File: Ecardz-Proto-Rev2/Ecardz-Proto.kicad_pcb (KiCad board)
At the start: 4 copper layers, 110 x 90 mm, 63 parts, among them IC1 M24LR04E-RMN6T/2, J1 Conn_02x06_Odd_Even, J2 Conn_01x24, J3 Conn_01x06, Q1 NMOS, U1 STM32L071K8Ux

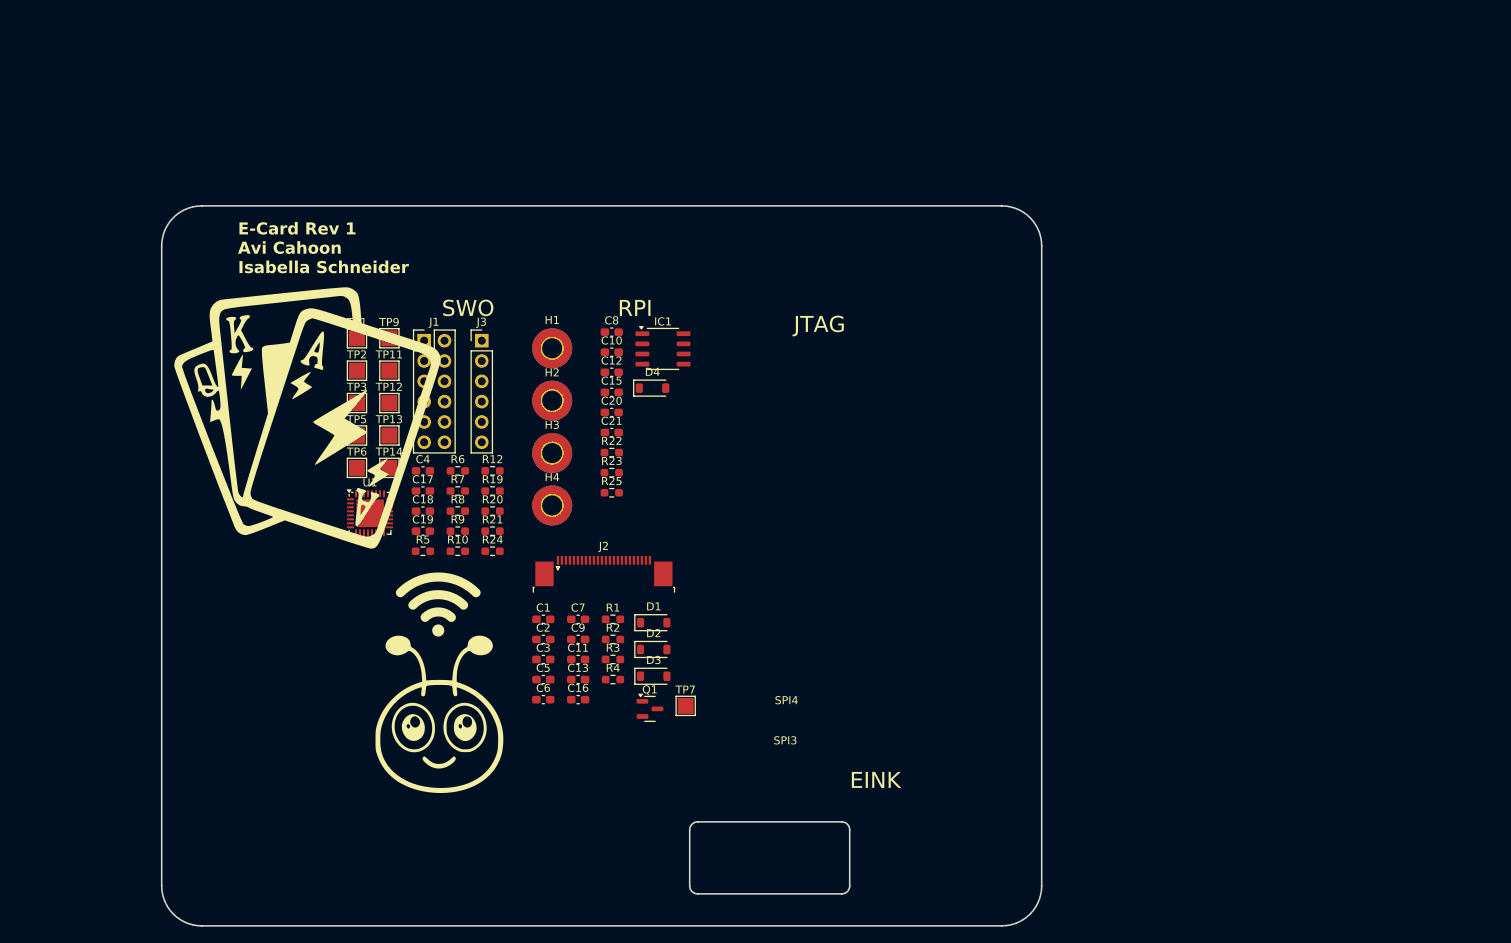
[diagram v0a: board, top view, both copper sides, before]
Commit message: Started board layout + antenna
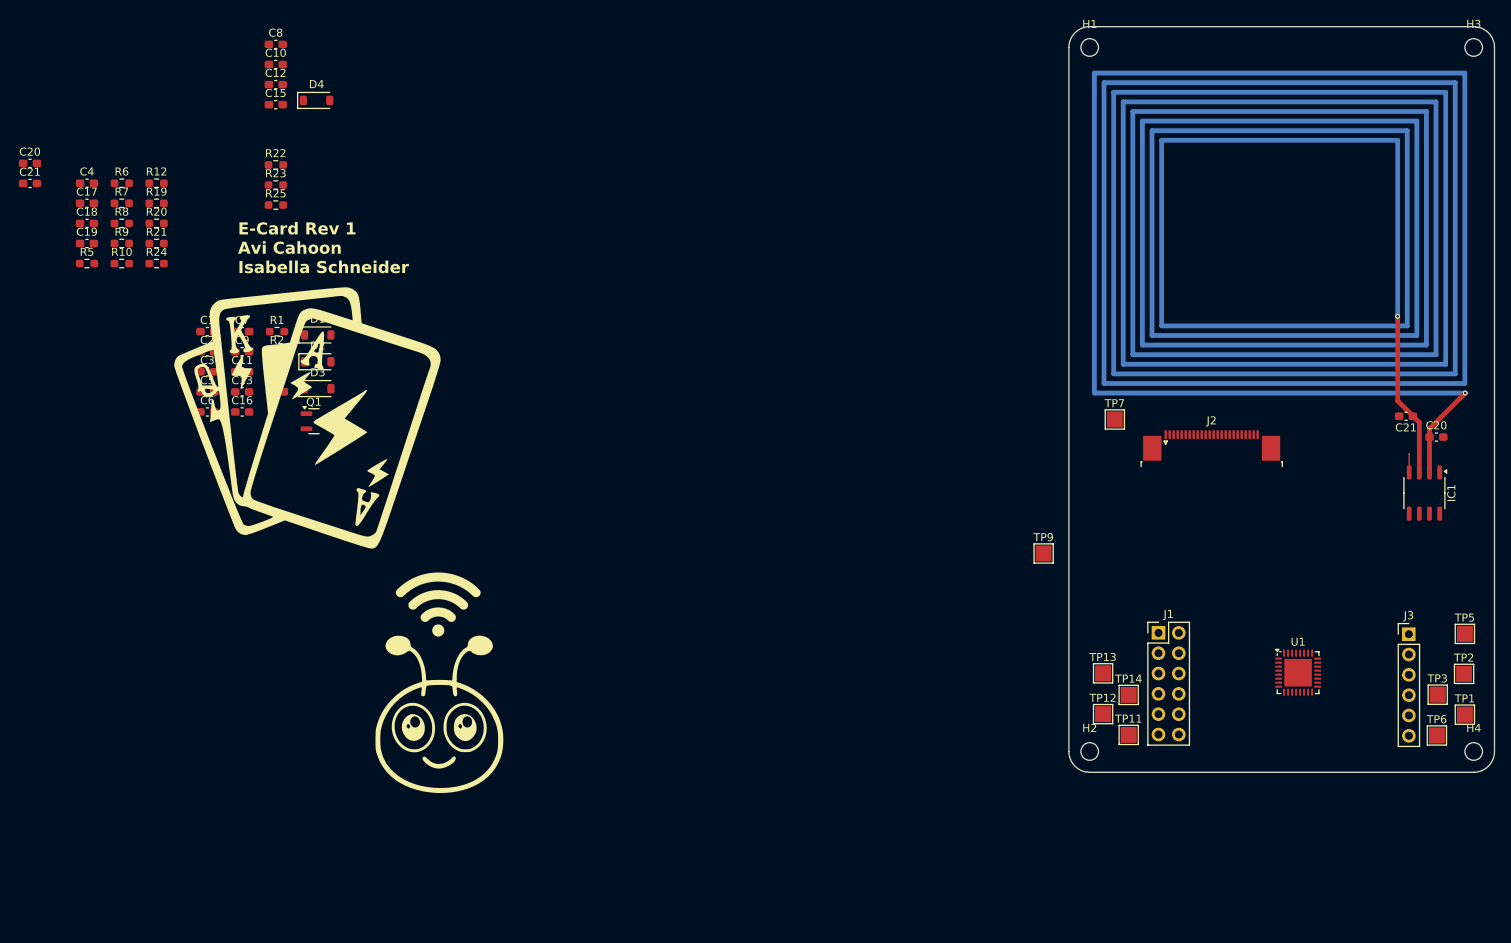
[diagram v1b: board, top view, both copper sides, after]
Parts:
- removed the C20 at (101.3, 70.8)
- removed the C21 at (101.3, 73.3)
- added C20: 7pF, Capacitor_SMD:C_0603_1608Metric_Pad1.08x0.95mm_HandSolder, F.Cu at (204.3, 73.9)
- added C20: 7pF, Capacitor_SMD:C_0603_1608Metric_Pad1.08x0.95mm_HandSolder, F.Cu at (28.5, 39.7)
- added C21: 7pF, Capacitor_SMD:C_0603_1608Metric_Pad1.08x0.95mm_HandSolder, F.Cu at (200.5, 71.3)
- added C21: 7pF, Capacitor_SMD:C_0603_1608Metric_Pad1.08x0.95mm_HandSolder, F.Cu at (28.5, 42.2)
- H1, H2, H3, H4: footprint MountingHole:MountingHole_2.5mm_Pad_TopBottom -> MountingHole:MountingHole_2.2mm_M2_DIN965
- moved TP1 146.3 mm to (207.9, 108.6)
- moved TP2 143.5 mm to (207.8, 103.5)
- moved TP5 140.7 mm to (207.9, 98.5)
- moved TP3 139.9 mm to (204.5, 106.1)
- moved TP6 139.1 mm to (204.4, 111.2)
- moved H3 125.9 mm to (209.0, 25.2)
- moved J3 121.6 mm to (200.9, 98.5)
- moved H4 119.2 mm to (209.0, 113.2)
- moved U1 117.7 mm to (187.1, 103.3)
- moved TP11 103.0 mm to (165.9, 111.1)
- moved J1 98.8 mm to (169.6, 98.4)
- moved TP12 97.3 mm to (162.7, 108.5)
- moved IC1 96.9 mm to (202.8, 80.9), turned to -90 degrees
- moved TP14 96.7 mm to (165.9, 106.1)
- moved TP13 94.0 mm to (162.7, 103.4)
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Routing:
- net Net-(IC1-AC0): track 0.00 -> 1143.3 mm, vias 0 -> 2
- net GND: track 0.00 -> 2.33 mm
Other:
- board size 110 x 90 mm -> 53.2 x 93.2 mm
- board text removed: "EINK"
- board text removed: "JTAG"
- board text removed: "RPI"
- board text removed: "SPI3"
- board text removed: "SPI4"
- board text removed: "SWO"

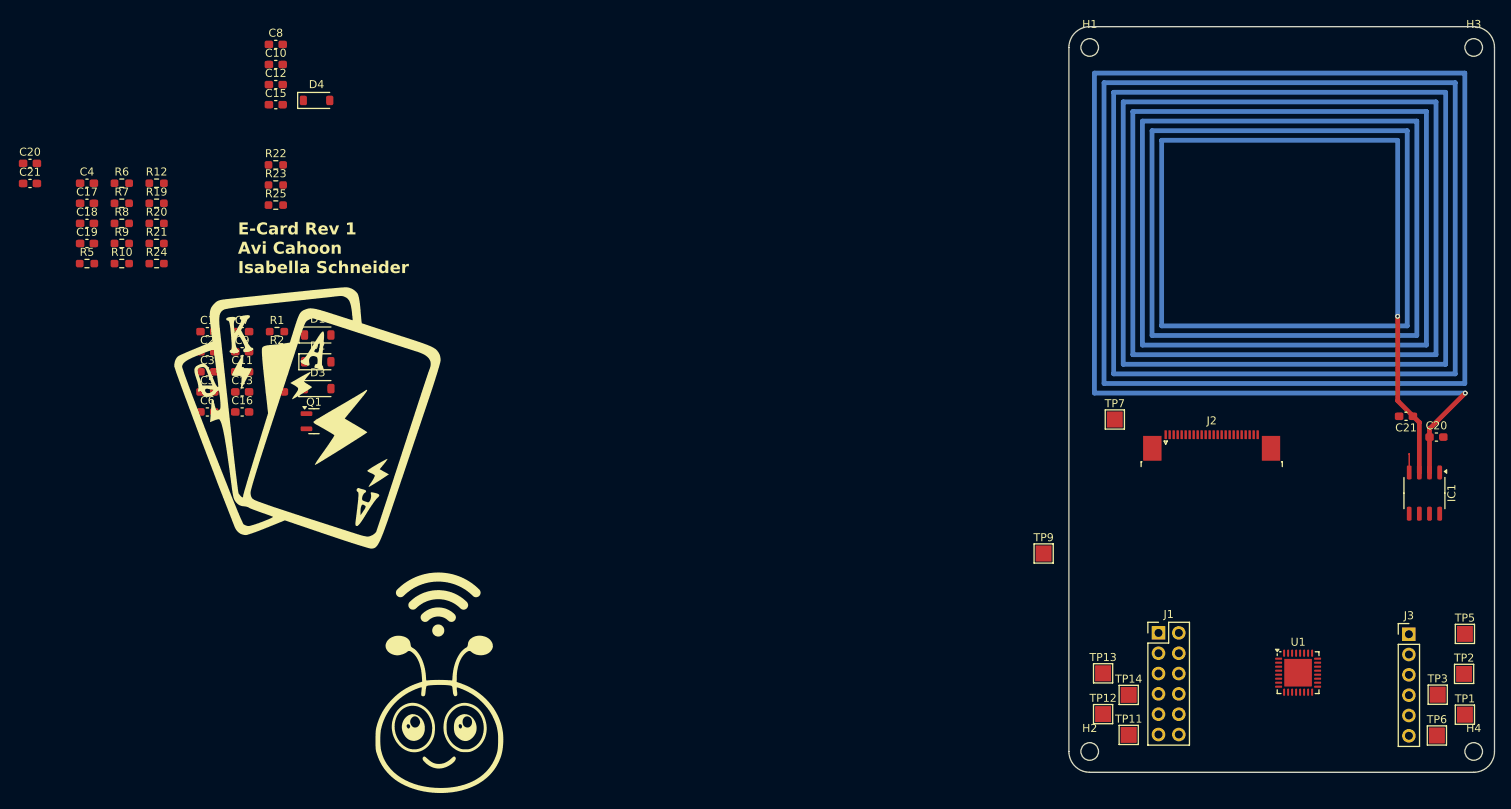
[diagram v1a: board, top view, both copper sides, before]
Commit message: most of layout complete
switched ADC pins for ease of layout. added LEDs
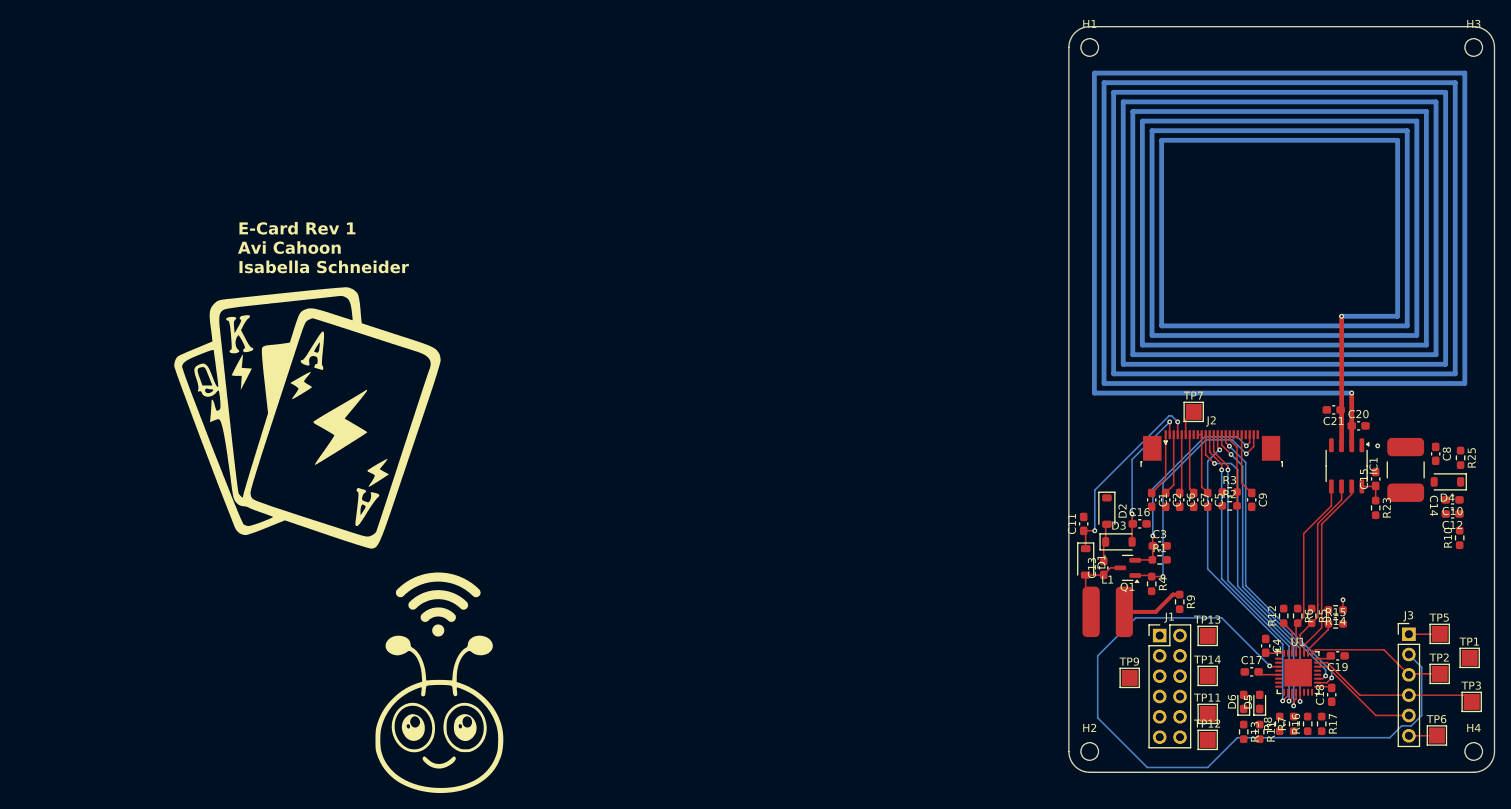
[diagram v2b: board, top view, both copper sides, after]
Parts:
- removed the C20 at (204.3, 73.9)
- removed the C20 at (28.5, 39.7)
- removed the C21 at (200.5, 71.3)
- removed the C21 at (28.5, 42.2)
- removed R19, R20, R21, R24: 10k, Resistor_SMD:R_0603_1608Metric_Pad0.98x0.95mm_HandSolder
- removed R22: DNP, Resistor_SMD:R_0603_1608Metric_Pad0.98x0.95mm_HandSolder
- added C14: TBD, parts-lib:C_2917, F.Cu at (200.5, 78.0)
- added C20: 7pF, Capacitor_SMD:C_0603_1608Metric_Pad1.08x0.95mm_HandSolder, F.Cu at (194.6, 72.5)
- added C21: 7pF, Capacitor_SMD:C_0603_1608Metric_Pad1.08x0.95mm_HandSolder, F.Cu at (191.5, 70.5)
- added D5: LED-G, LED_SMD:LED_0603_1608Metric_Pad1.05x0.95mm_HandSolder, F.Cu at (182.2, 107.0)
- added D6: LED-R, LED_SMD:LED_0603_1608Metric_Pad1.05x0.95mm_HandSolder, F.Cu at (180.2, 107.0)
- added L1: L, parts-lib:CDRH5D18, F.Cu at (163.2, 95.8)
- added R11: 10k, Resistor_SMD:R_0603_1608Metric_Pad0.98x0.95mm_HandSolder, F.Cu at (182.2, 110.8)
- added R13: 10k, Resistor_SMD:R_0603_1608Metric_Pad0.98x0.95mm_HandSolder, F.Cu at (180.2, 110.8)
- added R14: 10k, Resistor_SMD:R_0603_1608Metric_Pad0.98x0.95mm_HandSolder, F.Cu at (191.8, 95.5)
- added R15: 10k, Resistor_SMD:R_0603_1608Metric_Pad0.98x0.95mm_HandSolder, F.Cu at (191.8, 97.2)
- added R16: 10k, Resistor_SMD:R_0603_1608Metric_Pad0.98x0.95mm_HandSolder, F.Cu at (188.2, 109.8)
- added R17: 10k, Resistor_SMD:R_0603_1608Metric_Pad0.98x0.95mm_HandSolder, F.Cu at (190.0, 109.8)
- moved R10 170.7 mm to (207.2, 86.5), turned to 90 degrees
- moved C18 166.4 mm to (191.2, 106.1), turned to 90 degrees
- moved C19 164.6 mm to (192.0, 101.2), turned to 180 degrees
- moved R7 160.3 mm to (186.5, 109.8), turned to 90 degrees
- moved R5 159.3 mm to (188.8, 96.2), turned to -90 degrees
- moved C4 158.3 mm to (183.0, 100.0), turned to -90 degrees
- moved R8 157.7 mm to (184.8, 109.8), turned to 90 degrees
- moved C17 156.9 mm to (181.2, 103.2)
- moved C10 156.8 mm to (206.4, 81.8), turned to 180 degrees
- moved R6 156.6 mm to (187.0, 96.2), turned to -90 degrees
- moved C12 156.6 mm to (206.4, 83.5), turned to 180 degrees
- moved C8 153.8 mm to (204.2, 76.0), turned to -90 degrees
- moved R25 151.4 mm to (207.4, 76.5), turned to -90 degrees
- moved R12 150.9 mm to (185.2, 96.2), turned to 90 degrees
- moved D4 149.2 mm to (205.7, 79.5), turned to 180 degrees
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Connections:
- J1 pad 1: /EINK/SCL -> +3.3V
- J1 pad 10: /STM/NFC_BUSY -> /EINK/RES#
- J1 pad 11: /EINK/RES# -> GND
- J1 pad 12: GND -> /EINK/BUSY
- J1 pad 2: +3.3V -> /EINK/D/C#
- J1 pad 3: /EINK/SDA -> unconnected-(J1-Pin_3-Pad3)
- J1 pad 4: unconnected-(J1-Pin_4-Pad4) -> /EINK/CS#
- J1 pad 5: /EINK/D/C# -> /STM/NFC_BUSY
- J1 pad 6: /STM/I2C_NFC_SDA -> /EINK/CS#
- J1 pad 7: /EINK/CS# -> /STM/I2C_NFC_SCL
- J1 pad 8: /STM/I2C_NFC_SCL -> /EINK/SDA
- J1 pad 9: /EINK/BUSY -> /STM/I2C_NFC_SDA
- J2 pad 12: /EINK/SCL -> /EINK/CS#
- R8 pad 2: /EINK/SCL -> /EINK/CS#
- TP1 pad 1: /STM/SWO -> /STM/NRST
- U1 pad 11: /EINK/SCL -> /EINK/CS#
- U1 pad 15: unconnected-(U1-PB1-Pad15) -> /STM/VDD_MEAS
- U1 pad 26: unconnected-(U1-PB4-Pad26) -> /STM/EH_MEAS
- U1 pad 6: Net-(U1-PA0) -> /STM/INDICATOR_R
- U1 pad 7: /STM/VDD_MEAS -> /STM/INDICATOR_G
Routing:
- net VDD: track 124.7 -> 27.9 mm
- net /STM/NRST: track 0.00 -> 88.9 mm, vias 0 -> 1
- net /EINK/CS#: track 0.00 -> 78.6 mm, vias 0 -> 4
- net /EINK/SDA: track 0.00 -> 40.6 mm, vias 0 -> 2
- net /EINK/D/C#: track 0.00 -> 39.6 mm, vias 0 -> 2
- net /EINK/BUSY: track 0.00 -> 37.9 mm, vias 0 -> 2
- net /EINK/RES#: track 0.00 -> 36.7 mm, vias 0 -> 2
- net /EINK/GDR: track 0.00 -> 31.4 mm, vias 0 -> 2
- net /EINK/RESE: track 0.00 -> 27.5 mm, vias 0 -> 2
- net /EINK/VGH: track 0.00 -> 24.9 mm, vias 0 -> 2
- net /STM/NFC_BUSY: track 0.00 -> 23.3 mm
- net /STM/I2C_NFC_SCL: track 0.00 -> 23.0 mm
- net /STM/I2C_NFC_SDA: track 0.00 -> 22.7 mm
- net /STM/SWDIO: track 0.00 -> 21.3 mm
- net /EINK/VGL: track 0.00 -> 18.5 mm, vias 0 -> 2
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
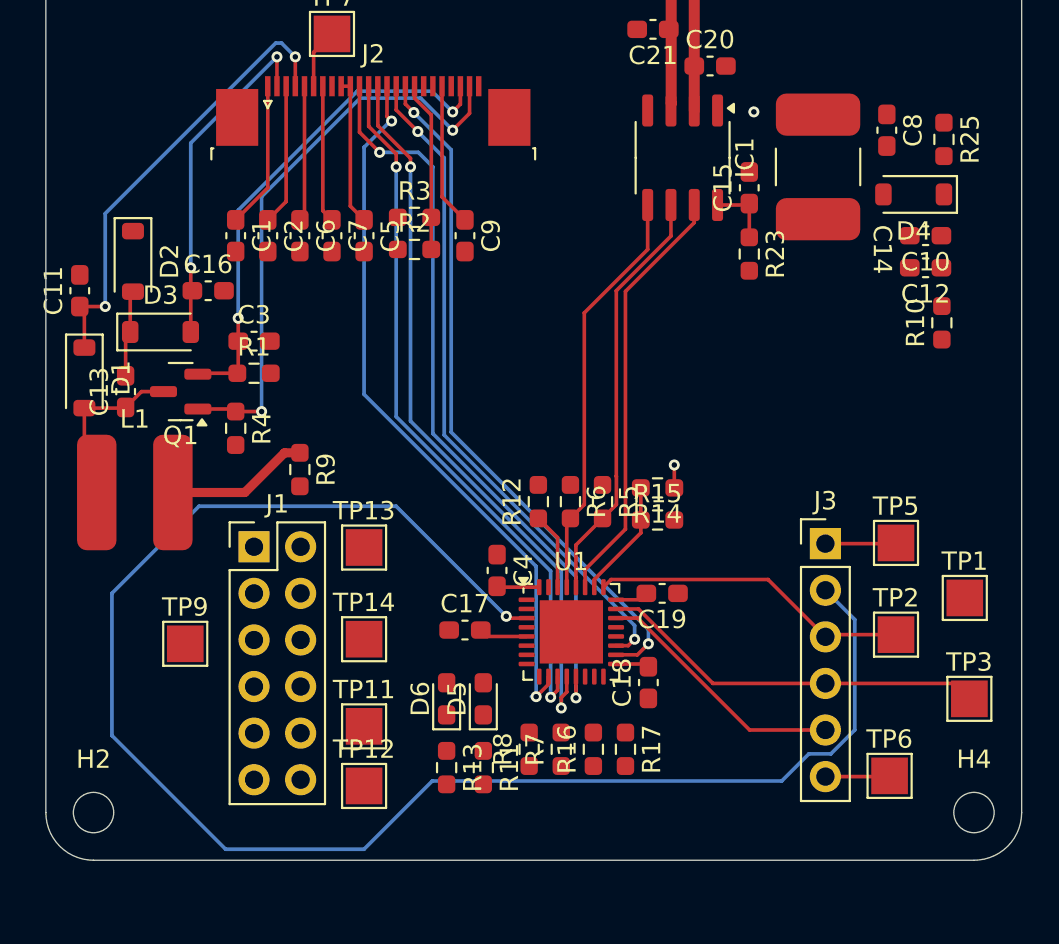
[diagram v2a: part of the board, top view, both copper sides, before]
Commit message: removed RPI header
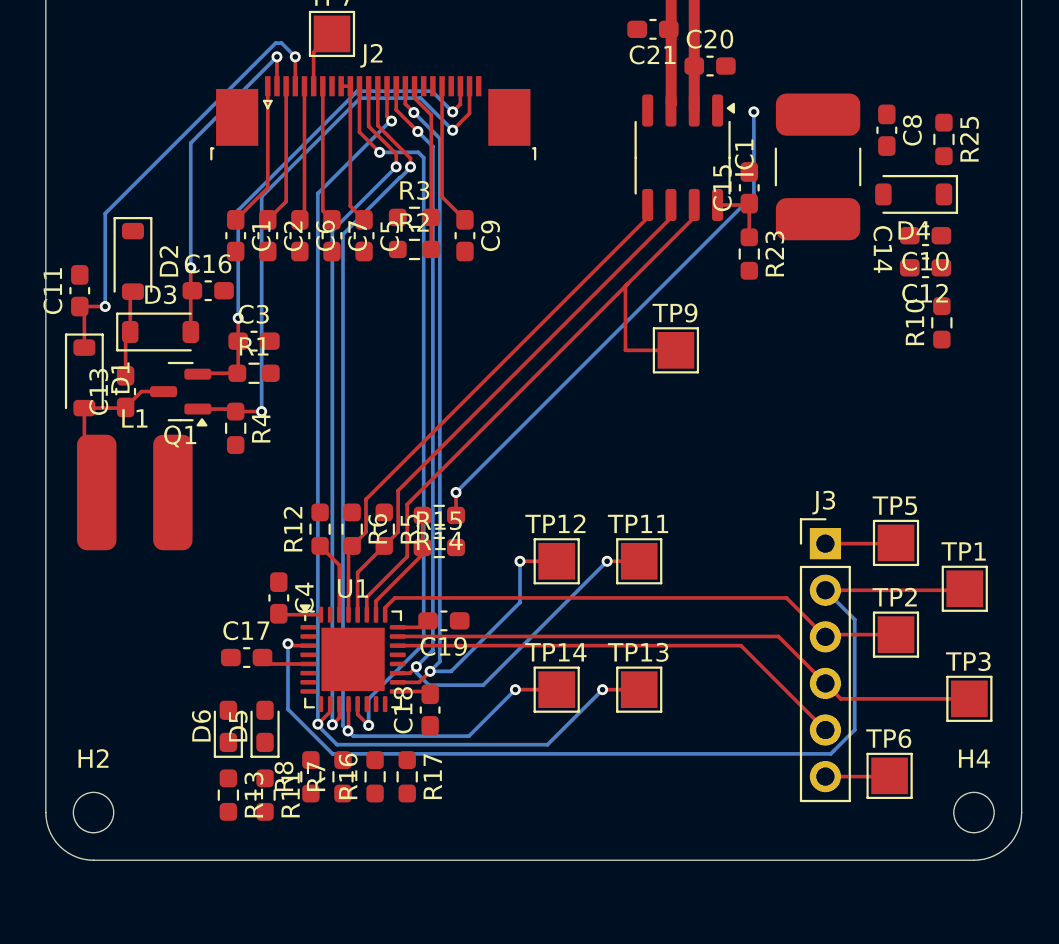
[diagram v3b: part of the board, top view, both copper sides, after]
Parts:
- removed J1: Conn_02x06_Odd_Even, Connector_PinHeader_2.54mm:PinHeader_2x06_P2.54mm_Vertical
- removed R9: DNP, Resistor_SMD:R_0603_1608Metric_Pad0.98x0.95mm_HandSolder
- moved TP9 31.2 mm to (192.8, 88.0)
- moved TP11 17.5 mm to (190.8, 99.5)
- moved TP13 16.9 mm to (190.8, 106.5)
- moved TP12 16.1 mm to (186.2, 99.5)
- moved C17 12.0 mm to (169.3, 104.8)
- moved C18 12.0 mm to (179.3, 107.6)
- moved C19 12.0 mm to (180.1, 102.8)
- moved C4 12.0 mm to (171.1, 101.5)
- moved D5 12.0 mm to (170.3, 108.5)
- moved D6 12.0 mm to (168.3, 108.5)
- moved R11 12.0 mm to (170.3, 112.2)
- moved R12 12.0 mm to (173.3, 97.8)
- moved R13 12.0 mm to (168.3, 112.2)
- moved R14 12.0 mm to (179.8, 97.0)
- moved R15 12.0 mm to (179.8, 98.8)
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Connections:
- J2 pad 12: /EINK/CS# -> /EINK/SCL
- R8 pad 2: /EINK/CS# -> /EINK/SCL
- U1 pad 11: /EINK/CS# -> /EINK/SCL
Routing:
- net /EINK/SCL: track 0.00 -> 38.2 mm, vias 0 -> 2
- net /STM/NRST: track 88.9 -> 53.6 mm
- net /NFC/V_E_HARVEST: track 1.25 -> 28.7 mm
- net /EINK/CS#: track 78.6 -> 51.6 mm, vias 4 -> 3
- net /EINK/D/C#: track 39.6 -> 57.2 mm, vias 2 -> 3
- net /EINK/RES#: track 36.7 -> 49.6 mm, vias 2 -> 3
- net /STM/NFC_BUSY: track 23.3 -> 36.2 mm
- net /STM/SWCLK: track 17.5 -> 29.4 mm
- net /STM/SWO: track 13.9 -> 25.2 mm
- net /STM/SWDIO: track 21.3 -> 32.6 mm
- net VDD: track 27.9 -> 20.1 mm
- net /EINK/BUSY: track 37.9 -> 45.6 mm, vias 2 -> 3
- net /STM/I2C_NFC_SDA: track 22.7 -> 29.1 mm
- net /STM/I2C_NFC_SCL: track 23.0 -> 29.4 mm
